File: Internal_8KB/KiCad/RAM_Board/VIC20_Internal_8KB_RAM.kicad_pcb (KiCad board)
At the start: 2 copper layers, 70 x 60 mm, 10 parts, among them J1 UD4, J2 UE4, J3 SW, J4 Signals, U1 6264, U2 GAL16V8

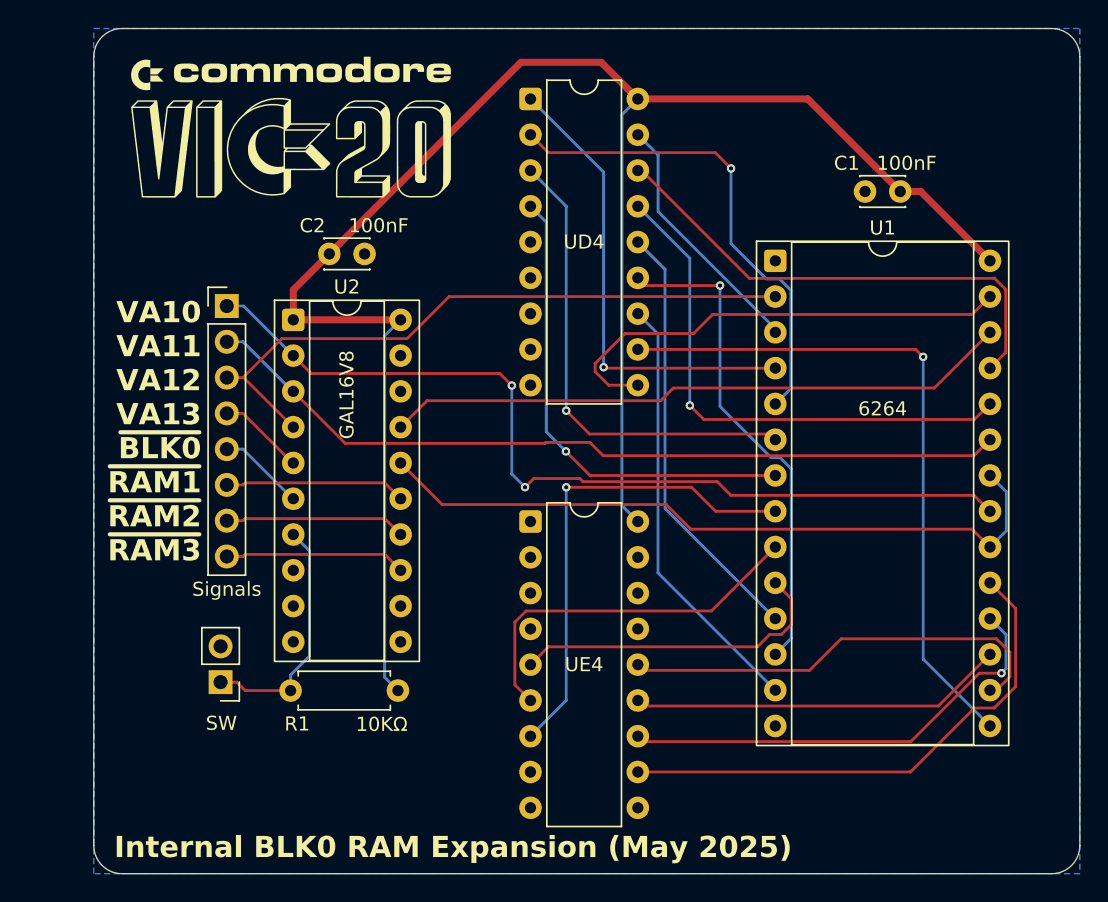
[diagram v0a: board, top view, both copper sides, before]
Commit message: Sent for test fabrication
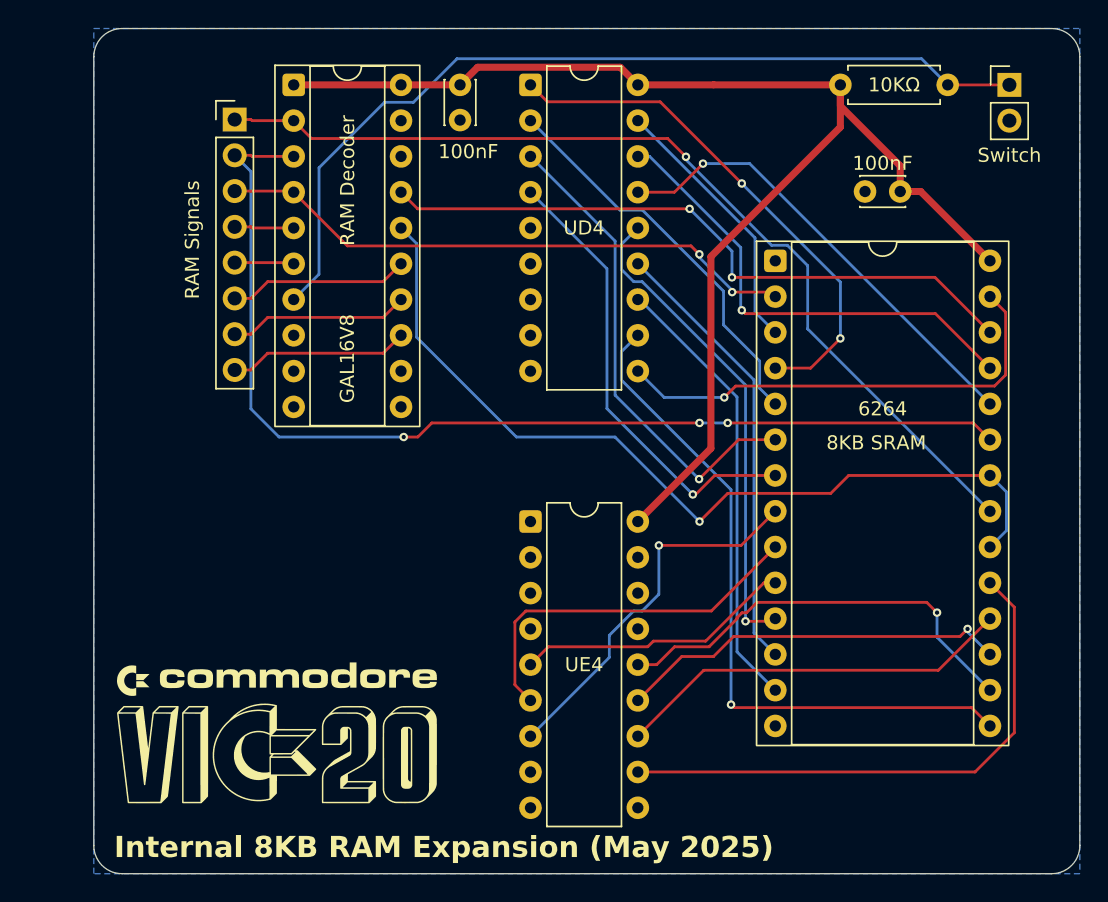
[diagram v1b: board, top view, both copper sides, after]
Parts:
- J3: value SW -> Switch
- J4: value Signals -> RAM Signals
- moved J3 70.2 mm to (114.0, 35.1), turned to 0 degrees
- moved R1 53.3 mm to (102.0, 35.1), turned to 0 degrees
- moved G*** 43.0 mm to (62.0, 81.1)
- moved U2 16.7 mm to (63.2, 35.1)
- moved C2 15.2 mm to (75.0, 35.1), turned to -90 degrees
- moved J4 13.3 mm to (59.0, 37.6)
- moved J1 1.00 mm to (80.0, 35.1)
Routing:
- net S: track 17.3 -> 63.1 mm
- net +5V: track 129.8 -> 94.5 mm
- net VA11: track 58.1 -> 76.9 mm, vias 0 -> 3
- net ~{CS1}: track 50.4 -> 61.7 mm, vias 0 -> 1
- net VA2: track 34.3 -> 26.9 mm
- net VA5: track 34.7 -> 28.2 mm, vias 1 -> 0
- net VA9: track 37.8 -> 32.9 mm
- net VA12: track 46.3 -> 41.7 mm, vias 0 -> 2
- net BD6: track 32.5 -> 28.5 mm, vias 1 -> 0
- net VA6: track 33.4 -> 37.3 mm, vias 1 -> 2
- net BD0: track 30.8 -> 34.6 mm, vias 0 -> 1
- net VA10: track 64.4 -> 67.9 mm, vias 2 -> 1
- net BD1: track 35.2 -> 31.8 mm, vias 1 -> 0
- net VA0: track 23.1 -> 19.8 mm
- net CS2: track 44.6 -> 47.0 mm, vias 0 -> 2
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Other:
- board text added: "8KB SRAM"
- board text added: "Brett Hallen, May 2025 Port Macquarie, Australia www.youtube.com/@Brfff"
- board text added: "Internal 8KB RAM Expansion (May 2025)"
- board text added: "RAM Decoder"
- board text removed: "Brett Hallen, Apr 2025 Port Macquarie, Australia www.youtube.com/@Brfff"
- board text removed: "Internal BLK0 RAM Expansion (May 2025)"
- board text removed: "VA10 VA11 VA12 VA13 ~{BLK0} ~{RAM1} ~{RAM2} ~{RAM3}"
